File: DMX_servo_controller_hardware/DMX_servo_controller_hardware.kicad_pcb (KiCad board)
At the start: 4 copper layers, 100 x 100 mm, 61 parts, among them J1 To_XLR3, J2 To_XLR3, J3 Power connector, J4 Display, J5 Rotary encoder, J6 Output block 1, J7 Output block 2, J8 Output block 3, J9 Output block 4, Q1 BSS138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

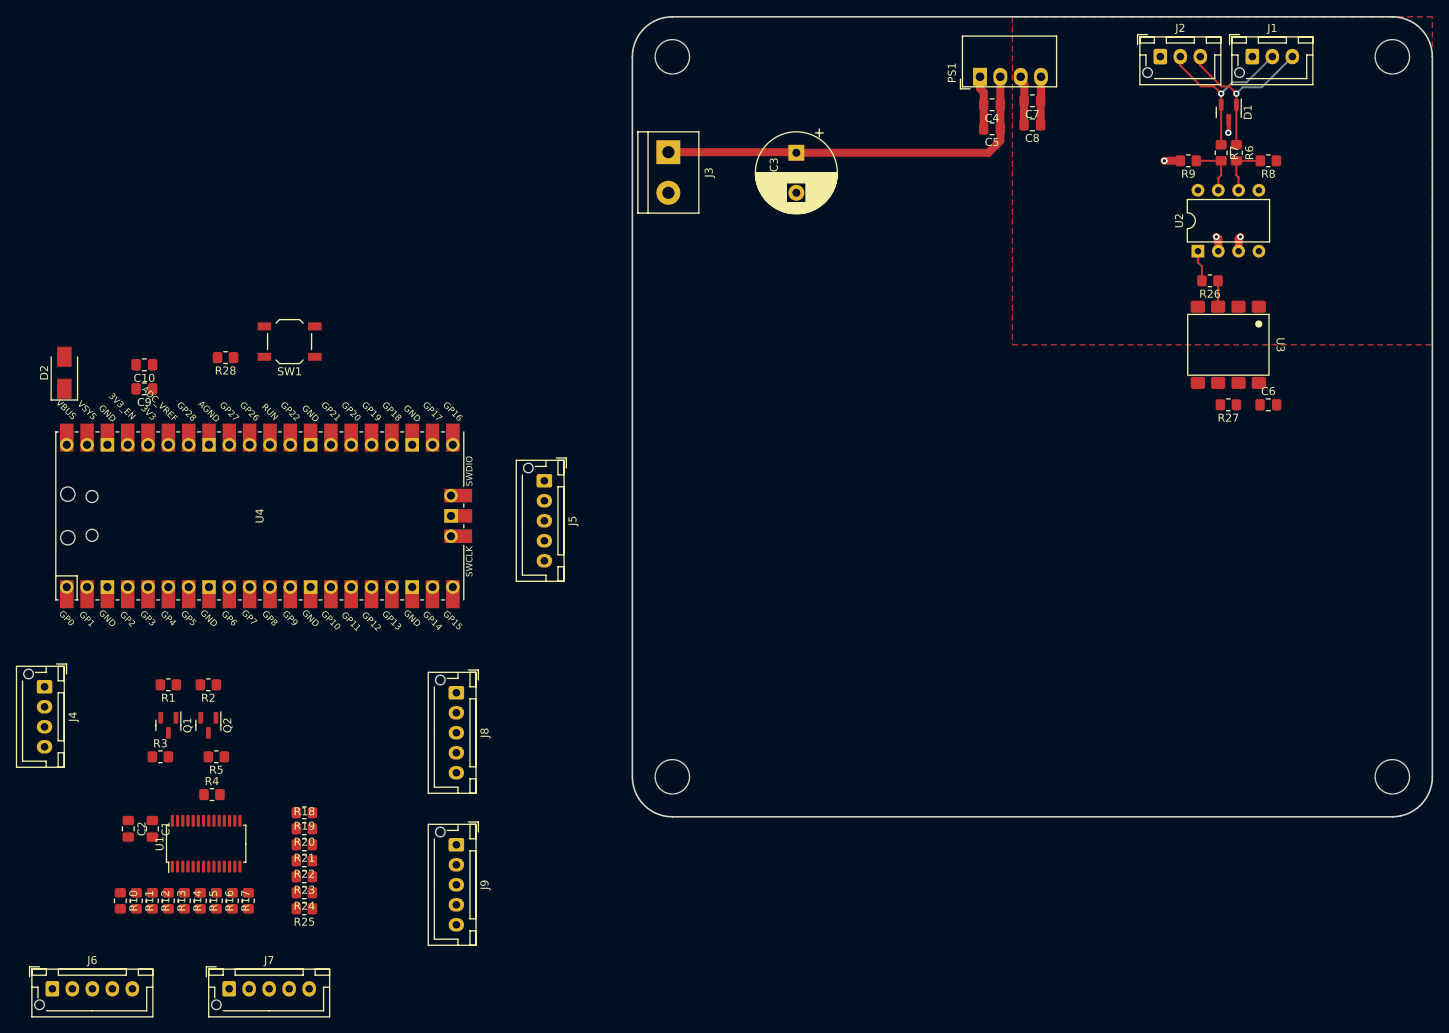
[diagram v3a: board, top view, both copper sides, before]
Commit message: Repositions rest of the components to route them in an easier way
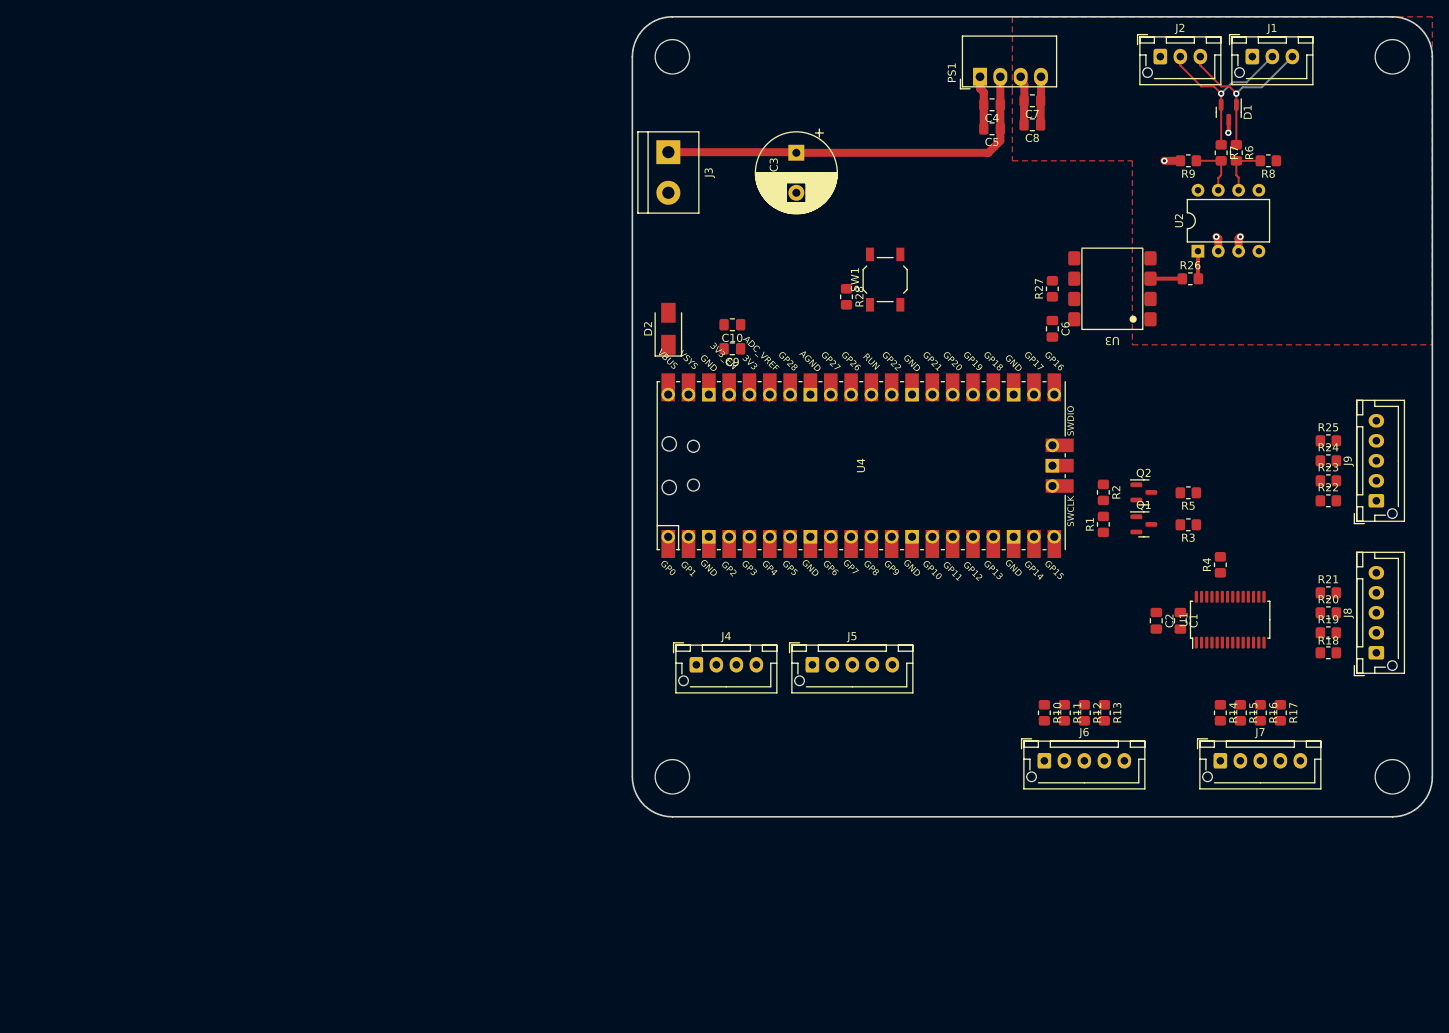
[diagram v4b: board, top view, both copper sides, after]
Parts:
- moved R25 140.7 mm to (187.0, 113.0), turned to 0 degrees
- moved R24 138.9 mm to (187.0, 115.5), turned to 0 degrees
- moved R18 138.5 mm to (187.0, 139.5), turned to 0 degrees
- moved R23 137.2 mm to (187.0, 118.0), turned to 0 degrees
- moved R22 135.7 mm to (187.0, 120.5), turned to 0 degrees
- moved R17 133.1 mm to (181.0, 147.0)
- moved R16 132.6 mm to (178.5, 147.0)
- moved R15 132.1 mm to (176.0, 147.0)
- moved R21 131.8 mm to (187.0, 132.0), turned to 0 degrees
- moved R3 131.7 mm to (169.5, 123.5), turned to 180 degrees
- moved R14 131.6 mm to (173.5, 147.0)
- moved C1 131.1 mm to (168.5, 135.5)
- moved C2 131.1 mm to (165.5, 135.5)
- moved U1 131.0 mm to (174.7, 135.4)
- moved R20 130.8 mm to (187.0, 134.5), turned to 0 degrees
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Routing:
- net Net-(U3-C): track 3.25 -> 3.99 mm

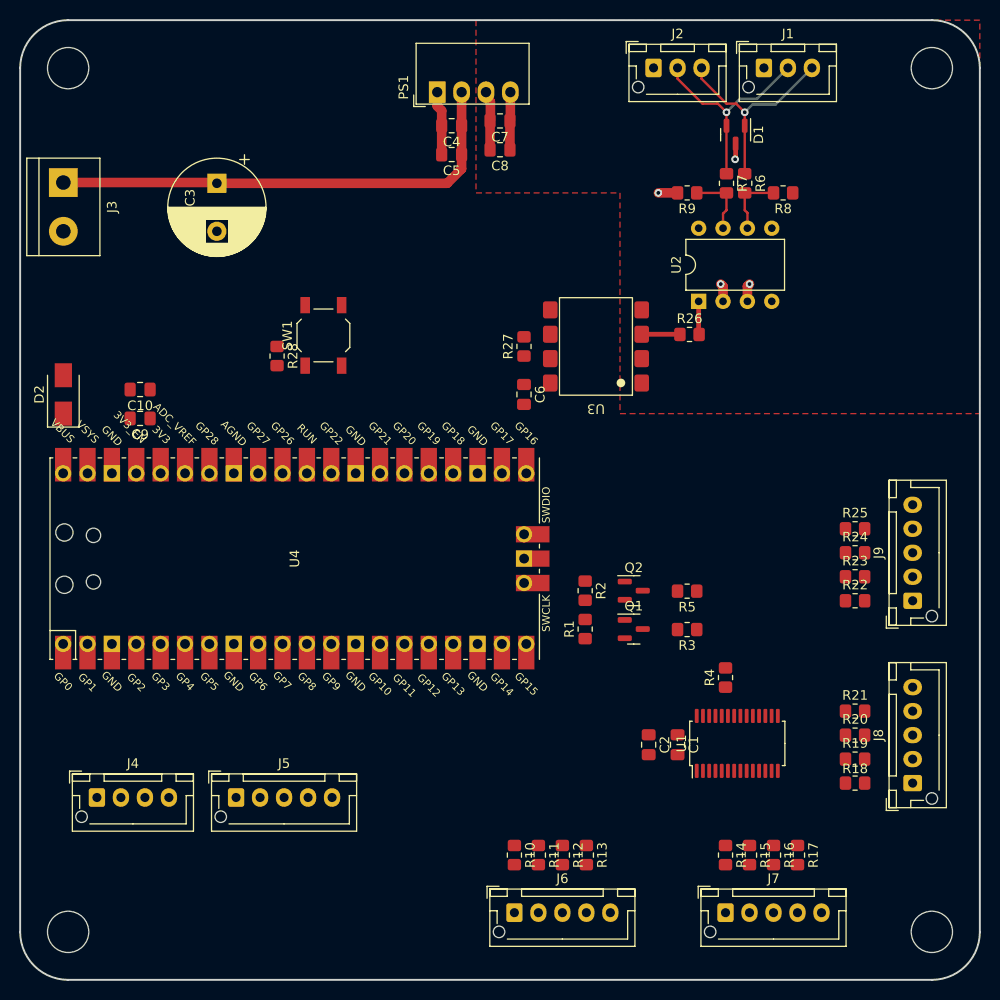
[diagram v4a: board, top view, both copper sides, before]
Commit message: First draft route for everything that was unrouted
There's definitely a lot to improve still, but all nets are connected.
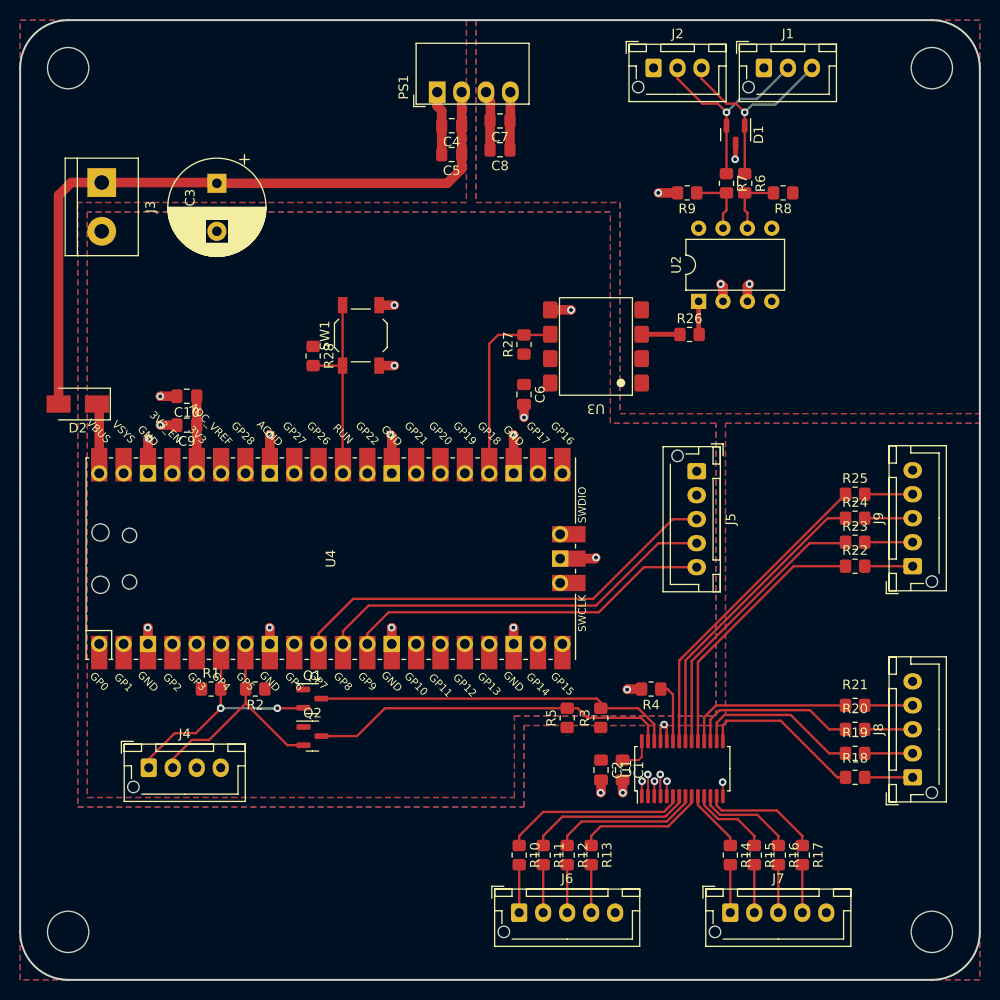
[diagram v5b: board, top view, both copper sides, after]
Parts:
- moved J5 58.8 mm to (170.5, 107.0), turned to -90 degrees
- moved R1 39.5 mm to (119.9, 129.7), turned to 0 degrees
- moved Q2 36.7 mm to (130.5, 134.6)
- moved R2 35.9 mm to (124.5, 129.7), turned to 180 degrees
- moved Q1 34.3 mm to (130.4, 130.7)
- moved R5 18.2 mm to (157.0, 132.7), turned to 90 degrees
- moved R3 12.9 mm to (160.5, 132.7), turned to 90 degrees
- moved R4 7.84 mm to (165.8, 129.7), turned to 180 degrees
- moved C1 6.30 mm to (162.8, 138.1)
- moved U1 6.30 mm to (169.0, 138.0)
- moved J4 6.23 mm to (113.4, 137.9)
- moved C2 5.62 mm to (160.5, 138.1)
- moved C10 4.91 mm to (117.4, 99.2)
- moved C9 4.91 mm to (117.4, 102.2)
- moved J3 4.00 mm to (108.5, 76.9)
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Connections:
- U4 pad 20: DMX_signal -> unconnected-(U4-GPIO15-Pad20)
- U4 pad 24: unconnected-(U4-GPIO18-Pad24) -> DMX_signal
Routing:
- net GND: track 6.69 -> 61.9 mm, vias 0 -> 25
- net Encoder SW: track 0.00 -> 45.4 mm
- net Encoder DT: track 0.00 -> 42.0 mm
- net Encoder CLK: track 0.00 -> 38.3 mm
- net Net-(Q1-D): track 0.00 -> 37.9 mm
- net Net-(Q2-D): track 0.00 -> 37.7 mm
- net Net-(U1-LED15): track 0.00 -> 32.9 mm
- net Net-(U1-LED14): track 0.00 -> 31.4 mm
- net Net-(U1-LED13): track 0.00 -> 29.5 mm
- net Net-(U1-LED12): track 0.00 -> 28.1 mm
- net I2C0_SDA: track 0.00 -> 28.1 mm, vias 0 -> 2
- net +5V: track 50.2 -> 76.7 mm
- net I2C0_SCL: track 0.00 -> 24.9 mm
- net RESET: track 0.00 -> 20.6 mm
- net DMX_signal: track 0.00 -> 20.3 mm
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- added copper zone on B.Cu, net +3.3V
- added copper zone on F.Cu, net +3.3V
- added copper zone on B.Cu, net +5V
- added copper zone on F.Cu, net +5V
- added copper zone on B.Cu, net +5VA
- added copper zone on In1.Cu, net GND
- added copper zone on In2.Cu, net GND

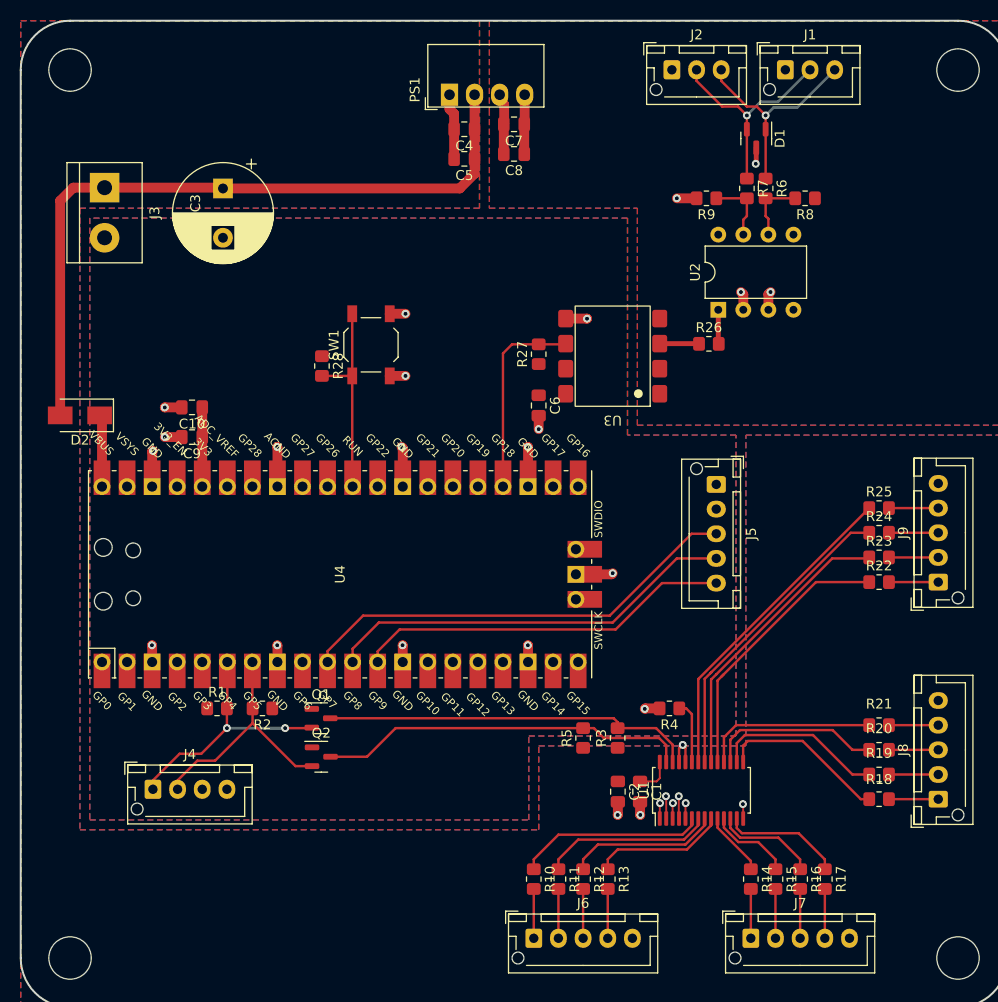
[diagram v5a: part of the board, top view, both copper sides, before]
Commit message: Edits some of the silkscreen an adjusts positioning slightly
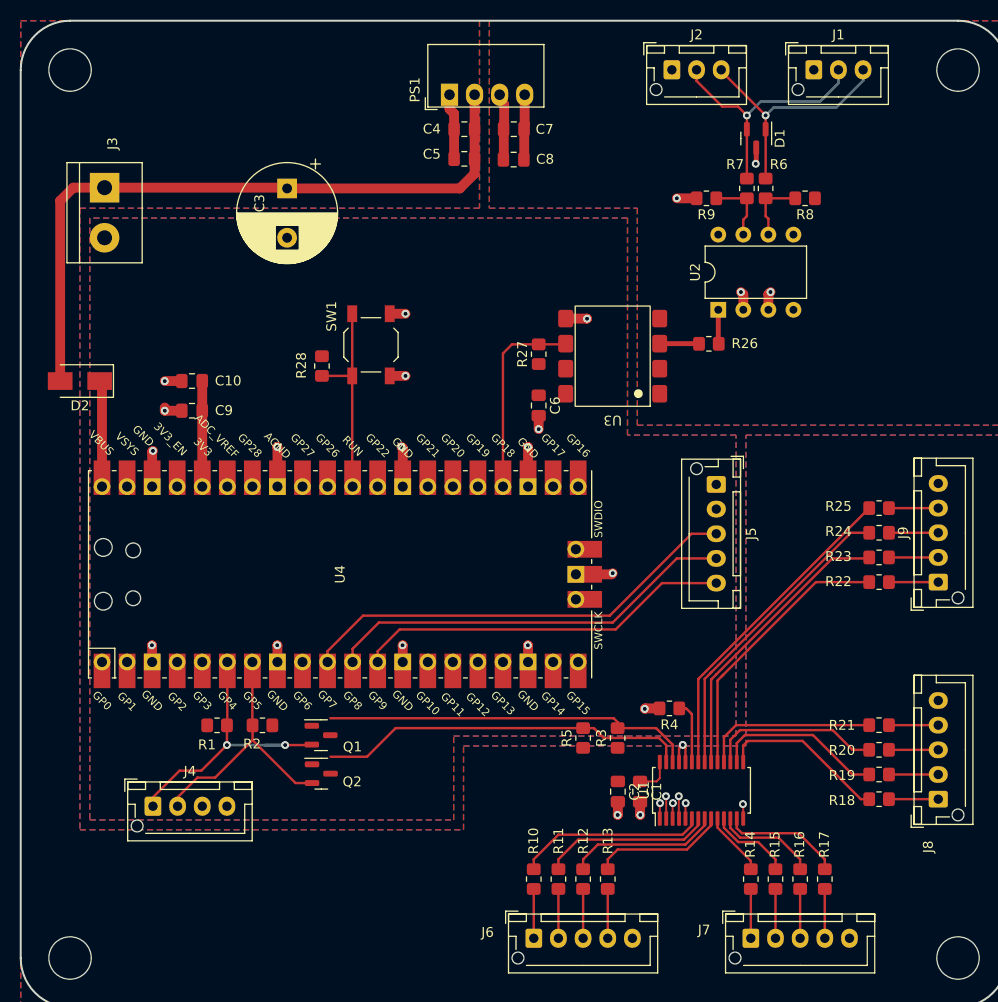
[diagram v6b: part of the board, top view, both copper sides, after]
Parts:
- moved C3 6.50 mm to (127.0, 77.0)
- moved D2 3.48 mm to (106.0, 96.5)
- moved J1 2.88 mm to (180.4, 65.0)
- moved C10 2.67 mm to (117.4, 96.5)
- moved C9 2.67 mm to (117.4, 99.5)
- moved Q1 1.72 mm to (130.4, 132.4)
- moved Q2 1.72 mm to (130.5, 136.3)
- moved R2 1.72 mm to (124.5, 131.4)
- moved R1 1.72 mm to (119.9, 131.4)
- moved J4 1.72 mm to (113.4, 139.6)
- moved C8 0.58 mm to (150.0, 74.1)
- moved C7 0.49 mm to (150.0, 71.0)
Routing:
- net DMX_positive/hot: track 22.4 -> 26.1 mm
- net +5V: track 76.7 -> 73.2 mm
- net Net-(D2-K): track 7.32 -> 10.8 mm
- net DMX_negative/cold: track 22.4 -> 25.4 mm
- net +3.3V: track 8.03 -> 10.7 mm
- net I2C0_SDA: track 28.1 -> 29.8 mm
- net I2C0_SCL: track 24.9 -> 26.7 mm

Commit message: Fixes DRC errors
There are a lot of warnings left, but the errors are fixed (for now).
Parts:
- moved J4 0.62 mm to (113.3, 139.0)
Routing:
- net Net-(Q2-D): track 37.7 -> 38.4 mm
- net Net-(Q1-D): track 37.9 -> 38.6 mm
- net I2C0_SDA: track 29.8 -> 29.2 mm
- net I2C0_SCL: track 26.7 -> 26.1 mm
- net +3.3V: vias 0 -> 3
